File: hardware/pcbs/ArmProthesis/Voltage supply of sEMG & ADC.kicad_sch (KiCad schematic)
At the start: 64 parts, among them Q1 BC817, Q2 BC817, Q3 BC817, U1 LT3045xMSE, U2 TPS7A4701RGWR, U3 LT8471EFE_TRPBF, U4 LT3094xMSE

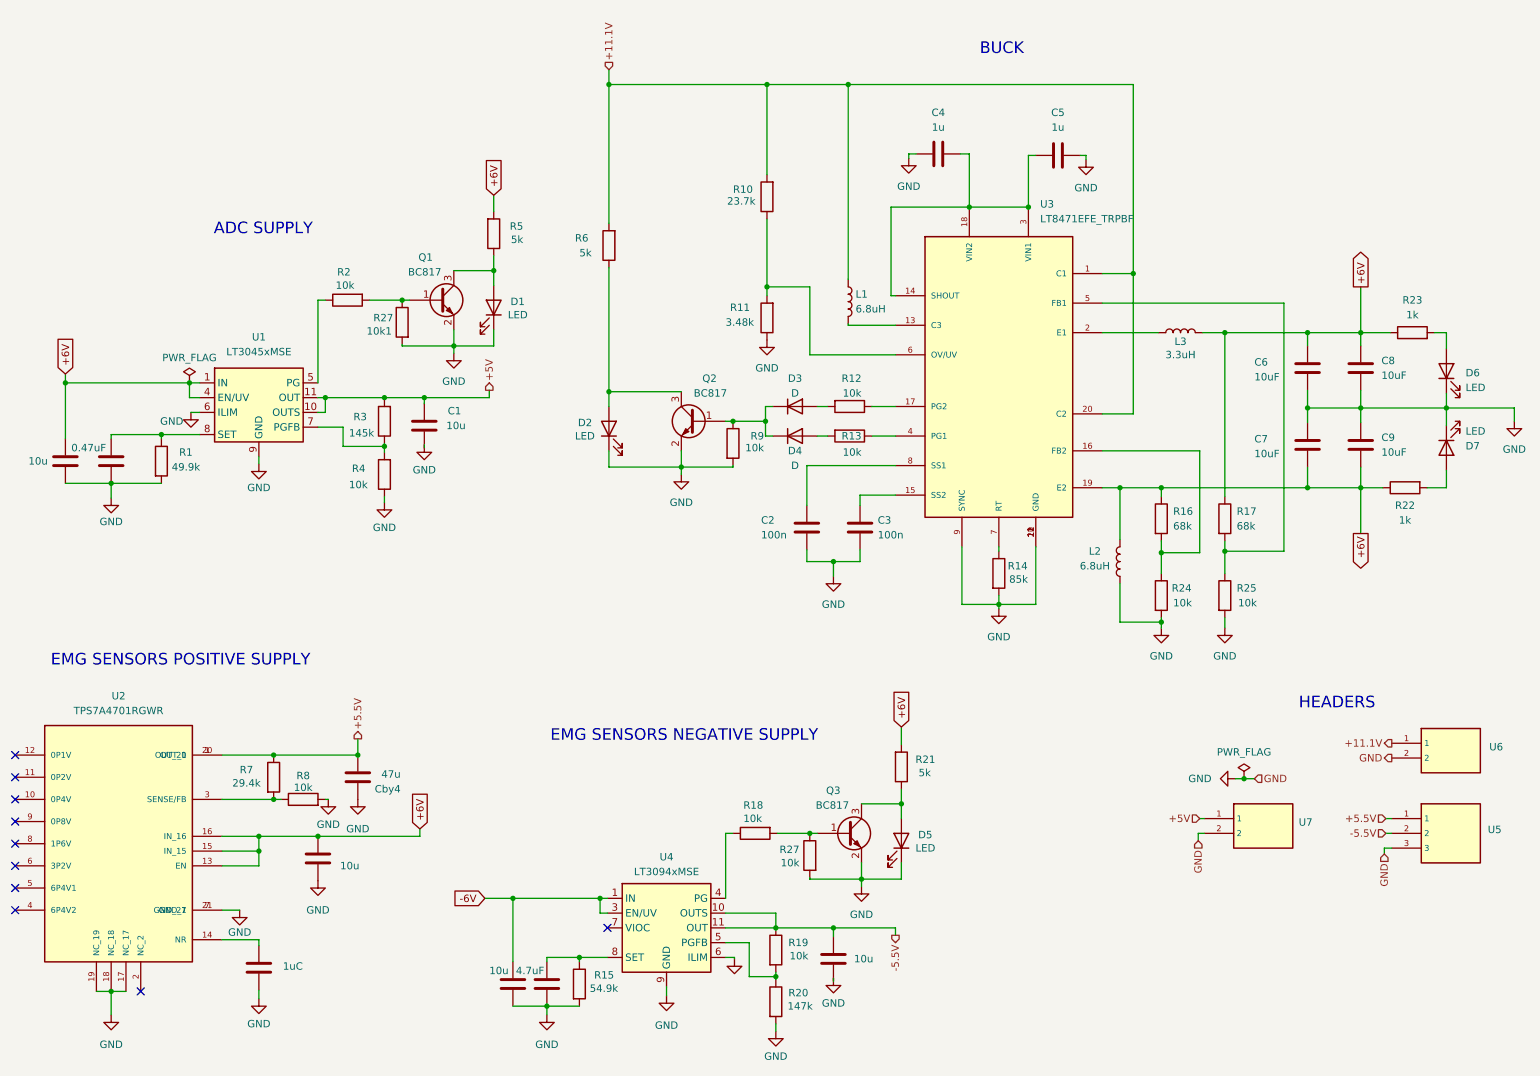
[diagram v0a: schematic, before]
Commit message: Voltage supply of sEMG & ADC
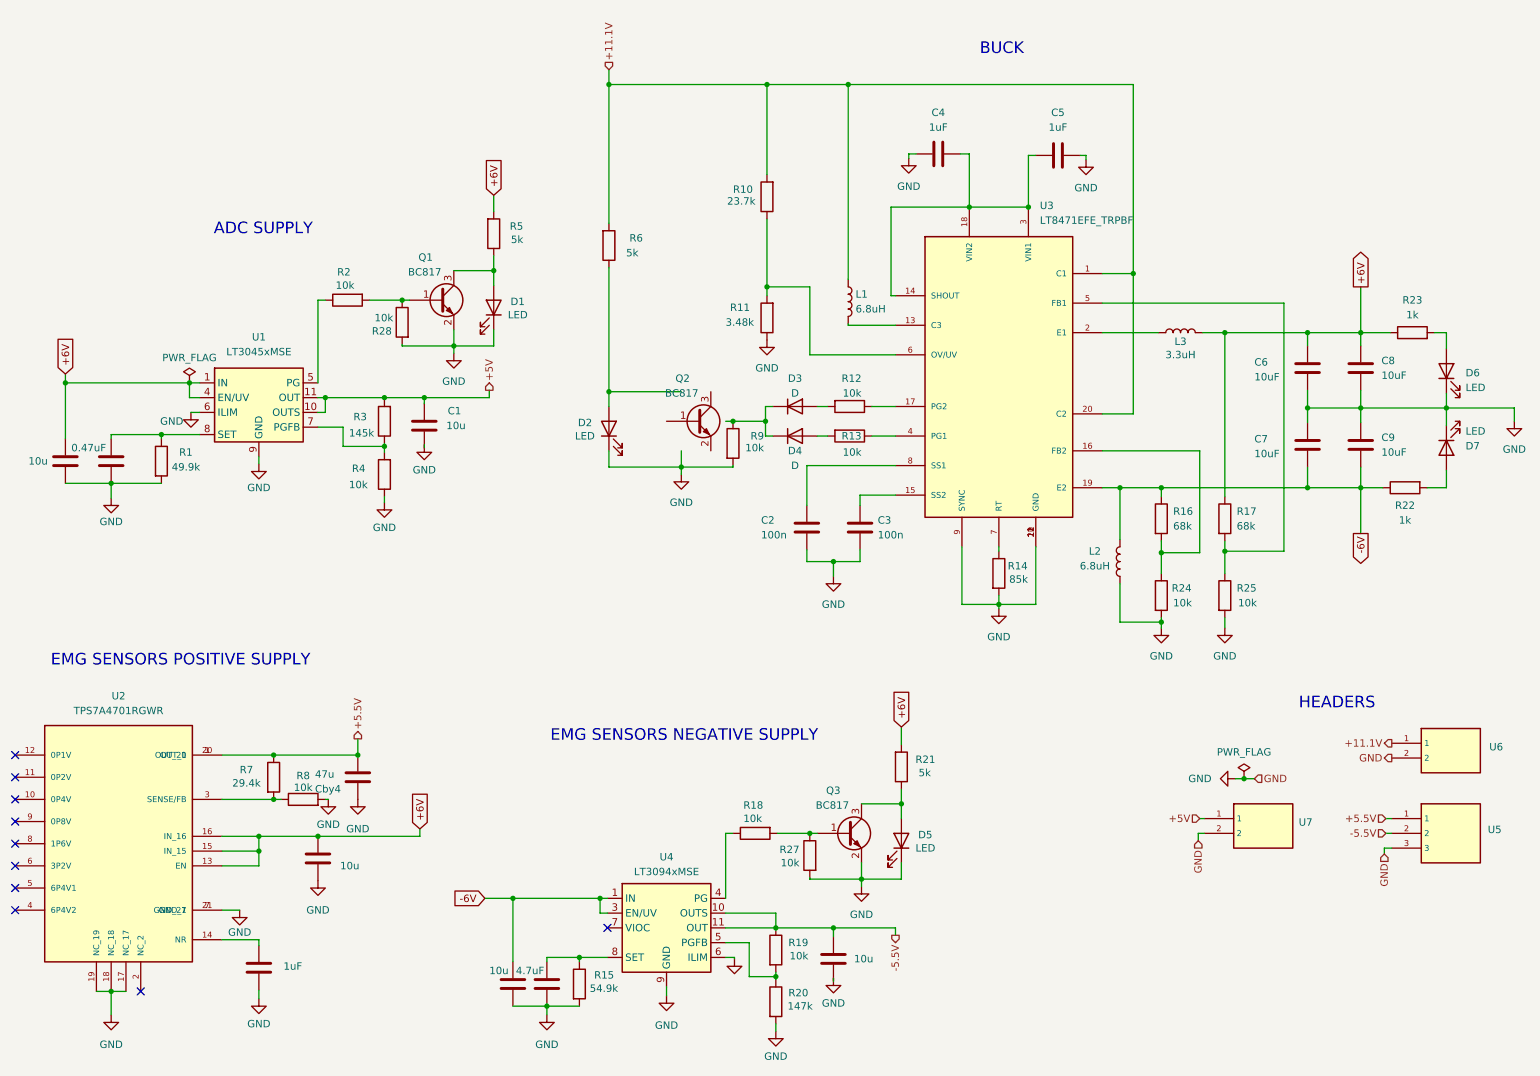
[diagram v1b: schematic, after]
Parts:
- C2, C3: footprint (none) -> Capacitor_SMD:C_0402_1005Metric_Pad0.74x0.62mm_HandSolder
- C2in1: value 1uC -> 1uF; footprint Capacitor_SMD:C_0603_1608Metric_Pad1.08x0.95mm_HandSolder -> Capacitor_SMD:C_0402_1005Metric_Pad0.74x0.62mm_HandSolder
- C4, C5: value 1u -> 1uF; footprint (none) -> Capacitor_SMD:C_0603_1608Metric_Pad1.08x0.95mm_HandSolder
- C6, C7, C8, C9: footprint (none) -> Capacitor_SMD:C_0805_2012Metric_Pad1.18x1.45mm_HandSolder
- D1, D2, D5, D6, D7: footprint (none) -> LED_SMD:LED_0603_1608Metric_Pad1.05x0.95mm_HandSolder
- D3, D4: footprint (none) -> Diode_SMD:D_SOD-123
- L1, L2: footprint (none) -> Inductor_SMD:L_Coilcraft_XAL7030-102
- L3: footprint (none) -> Inductor_SMD:L_Coilcraft_XAL5030-XXX
- R1, R15: footprint Resistor_SMD:R_0402_1005Metric_Pad0.72x0.64mm_HandSolder -> Resistor_SMD:R_0603_1608Metric_Pad0.98x0.95mm_HandSolder
- R11, R14, R20, R21, R22, R23, R3, R5, R6: footprint (none) -> Resistor_SMD:R_0603_1608Metric_Pad0.98x0.95mm_HandSolder
- R12, R13, R18, R19, R2, R4, R9: footprint (none) -> Resistor_SMD:R_0402_1005Metric_Pad0.72x0.64mm_HandSolder
- R28: renamed from 10k1; value R27 -> 10k
- U3: footprint BUCK:LT8471EFE -> BUCK:SOP65P640X120-21N
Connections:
- net +6V: no longer C7.2, C9.2, L2.2, R16.1, R22.1, U3.19 (E2)
- net -6V: now also C7.2, C9.2, L2.2, R16.1, R22.1, U3.19 (E2)
- net GND: no longer Q2.2 (E)
- net at D2.2 (A), R6.1: no longer Q2.3 (C)
- net at D3.1 (K), D4.1 (K), R9.1: no longer Q2.1 (B)
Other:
- moved on the sheet: Q2, R6

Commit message: BMS v0.2v + polishment of Vsupply  board
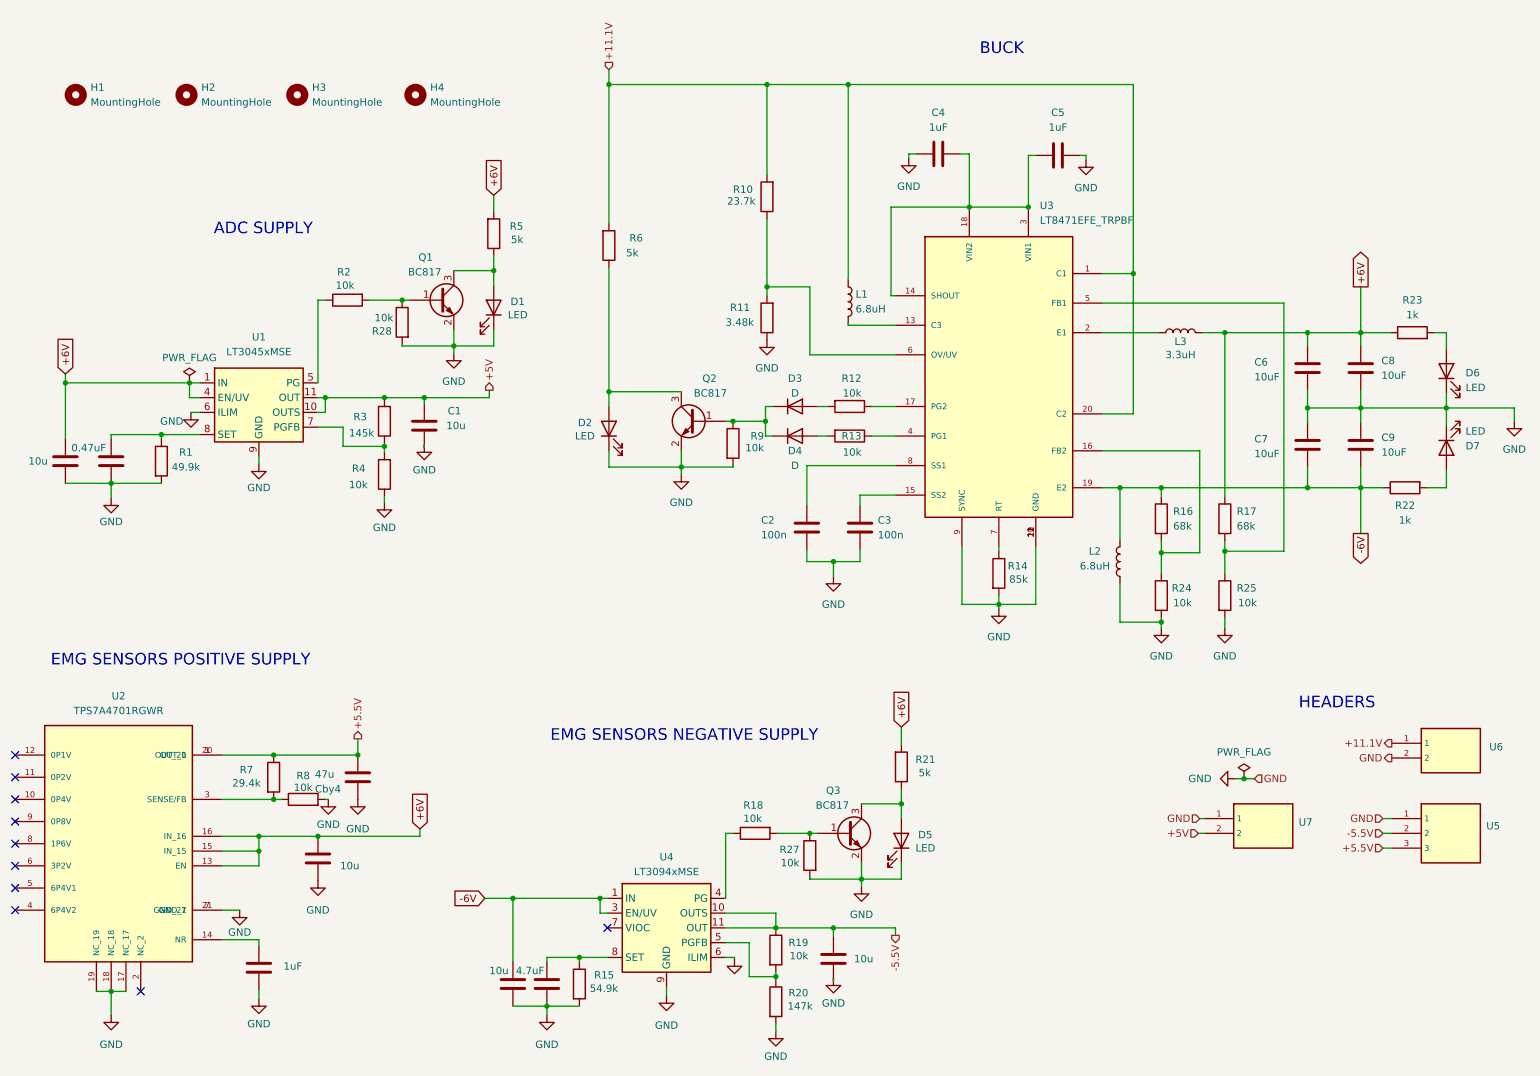
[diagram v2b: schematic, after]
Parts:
- added H1, H2, H3, H4: MountingHole, MountingHole:MountingHole_2.7mm_M2.5_DIN965, symbol Mechanical:MountingHole
- U5: footprint Connector_JST:JST_GH_BM03B-GHS-TBT_1x03-1MP_P1.25mm_Vertical -> Connector_JST:JST_GH_SM03B-GHS-TB_1x03-1MP_P1.25mm_Horizontal
- U6, U7: footprint Connector_JST:JST_GH_BM02B-GHS-TBT_1x02-1MP_P1.25mm_Vertical -> Connector_JST:JST_GH_SM02B-GHS-TB_1x02-1MP_P1.25mm_Horizontal
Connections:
- net +5.5V: now also U5.3; no longer U5.1
- net +5V: now also U7.2; no longer U7.1
- net GND: now also Q2.2 (E), U5.1, U7.1; no longer U5.3, U7.2
- net at D2.2 (A), R6.1: now also Q2.3 (C)
- net at D3.1 (K), D4.1 (K), R9.1: now also Q2.1 (B)
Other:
- moved on the sheet: Q2

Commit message: updates
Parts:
- added D8: DFLS240L, Diode_SMD:D_PowerDI-123, symbol Device:D_Schottky
- added D9: DFLS240, Diode_SMD:D_PowerDI-123, symbol Device:D_Schottky
- C1, Cby1, Cby3, Cby5, Cby7: value 10u -> 10uF; LCSC (none) -> C380332
- C2, C3: value 100n -> 100nF; LCSC (none) -> C514175
- C2in1: LCSC (none) -> C189893
- C4, C5: LCSC (none) -> C181151
- C6, C7, C8, C9: LCSC (none) -> C380332
- Cby2: LCSC (none) -> C666588
- Cby4: value 47u -> 47uF; LCSC (none) -> C580047
- Cby6: LCSC (none) -> C90084
- D1, D2, D5, D6, D7: LCSC (none) -> C107992
- D3, D4: LCSC (none) -> C25744
- L1, L2: LCSC (none) -> C114613
- L3: LCSC (none) -> C22878
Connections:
- net -6V: now also D9.2 (A); no longer L2.2, R16.1, U3.19 (E2)
- net GND: now also D8.2 (A)
- net at L3.1, U3.2 (E1): now also D8.1 (K)
- new net: D9.1 (K), L2.2, R16.1, U3.19 (E2)

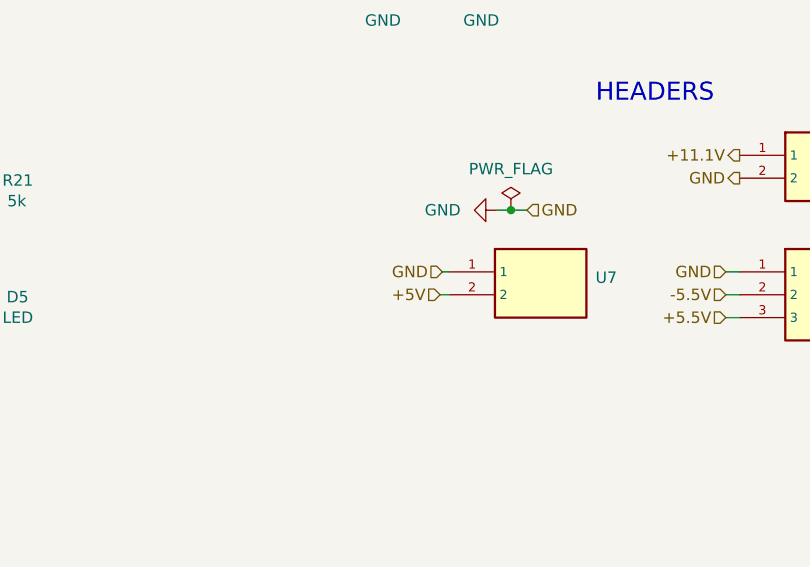
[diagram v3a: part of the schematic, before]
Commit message: Fix Vsupply
added important Schottky diodes on the BUCK
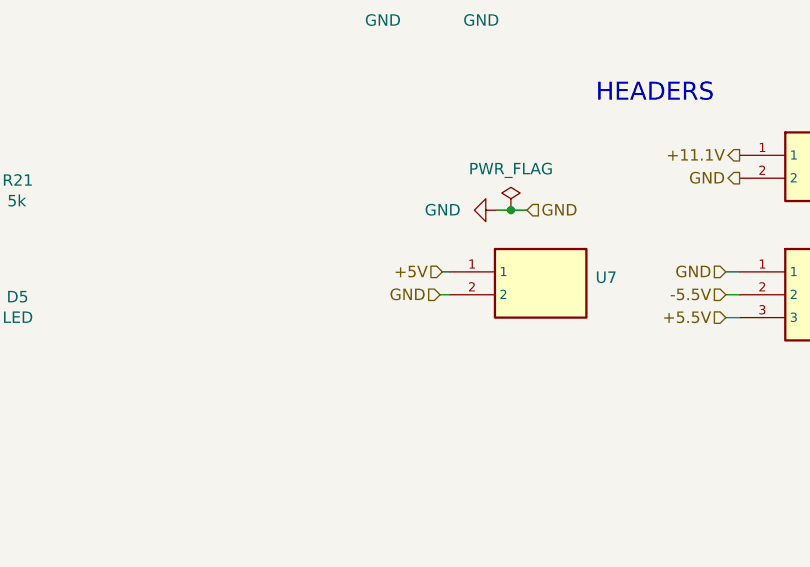
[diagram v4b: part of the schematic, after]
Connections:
- net +5V: now also U1.12 (OUT), U7.1; no longer U7.2
- net GND: now also U7.2; no longer U7.1
- net at R2.1, U1.5 (PG): no longer U1.12 (OUT)
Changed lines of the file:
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@@
 	(hierarchical_label "GND"
 		(shape input)
-		(at 223.774 152.4 180)
+		(at 223.52 154.94 180)
 		(effects
 			(font
@@
 	(hierarchical_label "+5V"
 		(shape input)
-		(at 223.52 154.94 180)
+		(at 223.774 152.4 180)
 		(effects
 			(font
